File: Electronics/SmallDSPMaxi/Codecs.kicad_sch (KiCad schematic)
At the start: 56 parts, among them J13 IDC, J14 IDC, J15 IDC, J16 IDC

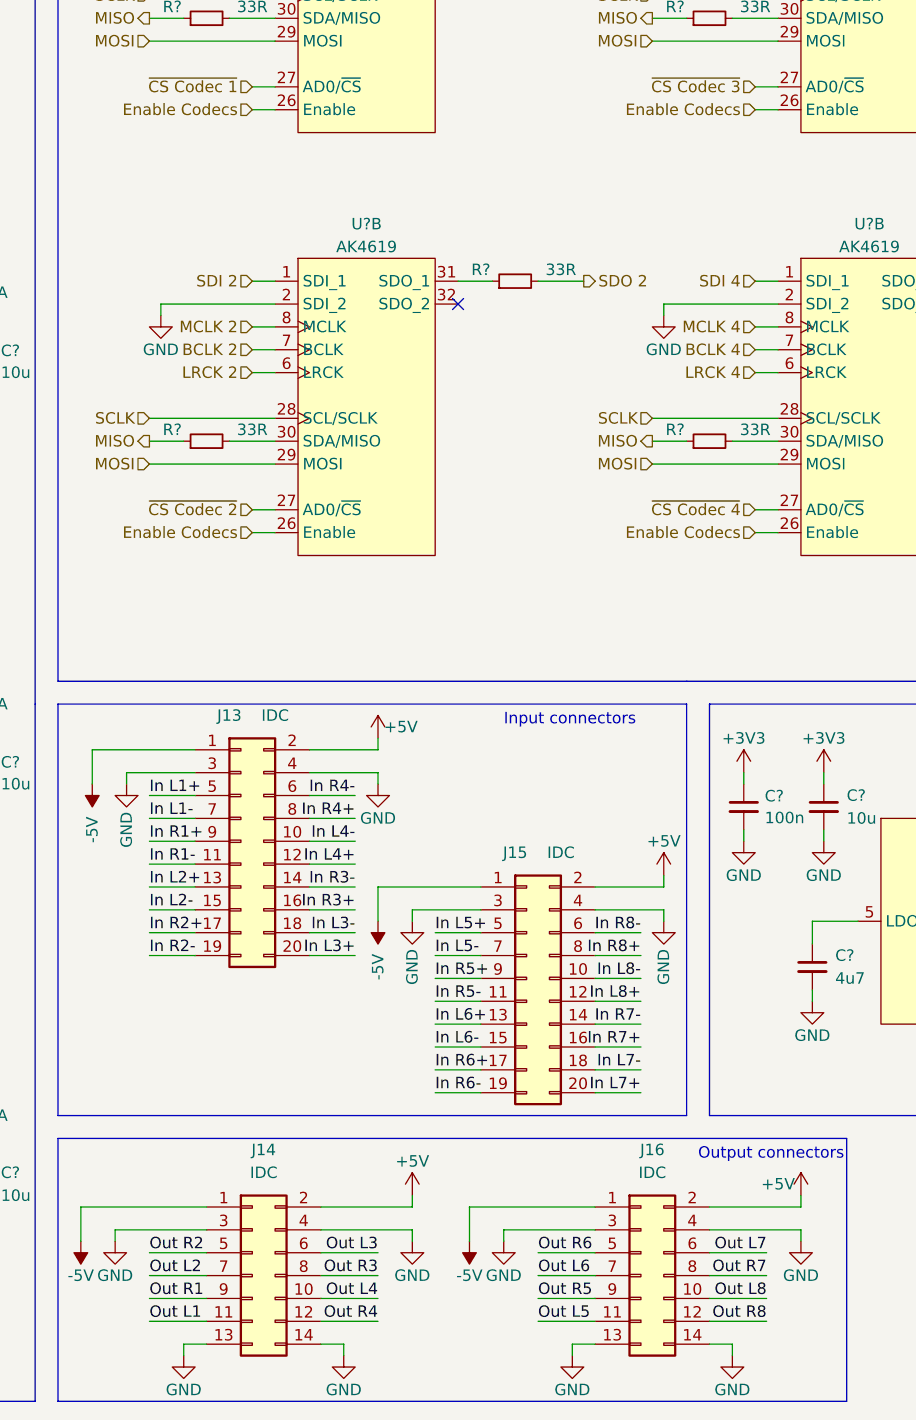
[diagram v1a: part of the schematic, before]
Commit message: Maxi: Replaces STM32 programming pin header with WE RedFit connectorand fixes minor issues. Adds driver for AKM AK4619 Codec and STM32CubeIDE workspace for Maxi firmware.
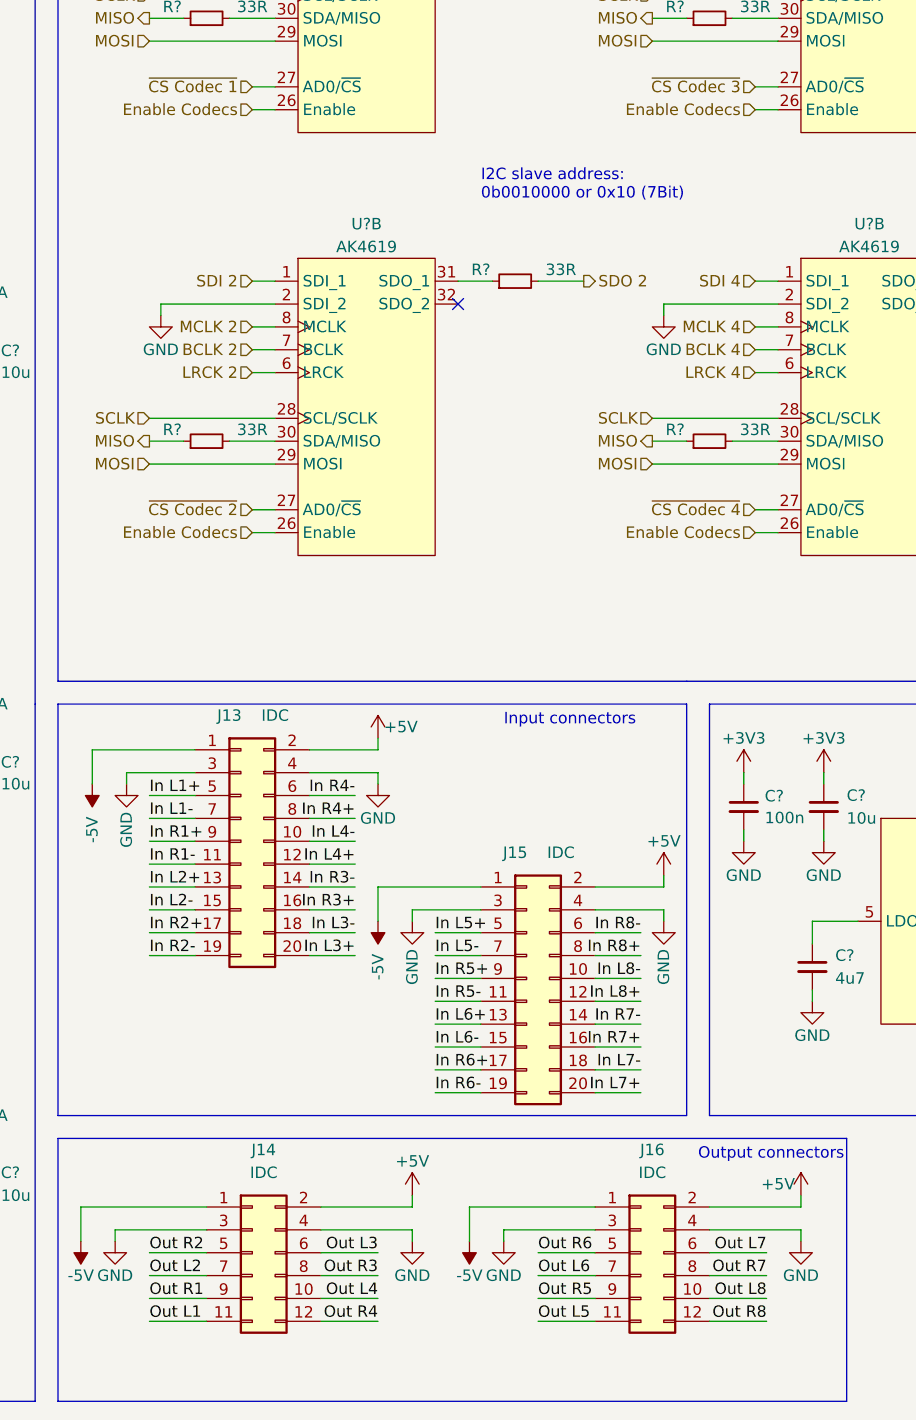
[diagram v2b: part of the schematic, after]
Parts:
- J14, J16: footprint Connector_IDC:IDC-Header_2x07_P2.54mm_Vertical -> Connector_IDC:IDC-Header_2x06_P2.54mm_Vertical; symbol Connector_Generic:Conn_02x07_Odd_Even -> Connector_Generic:Conn_02x06_Odd_Even
- U? (x12): LCSC Part # - -> C3034747; Notes (none) -> LCSC not in stock
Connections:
- net GND: no longer J14.13 (Pin_13), J14.14 (Pin_14), J16.13 (Pin_13), J16.14 (Pin_14)
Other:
- note added: "I2C slave address: 0b0010000 or 0x10 (7Bit)"

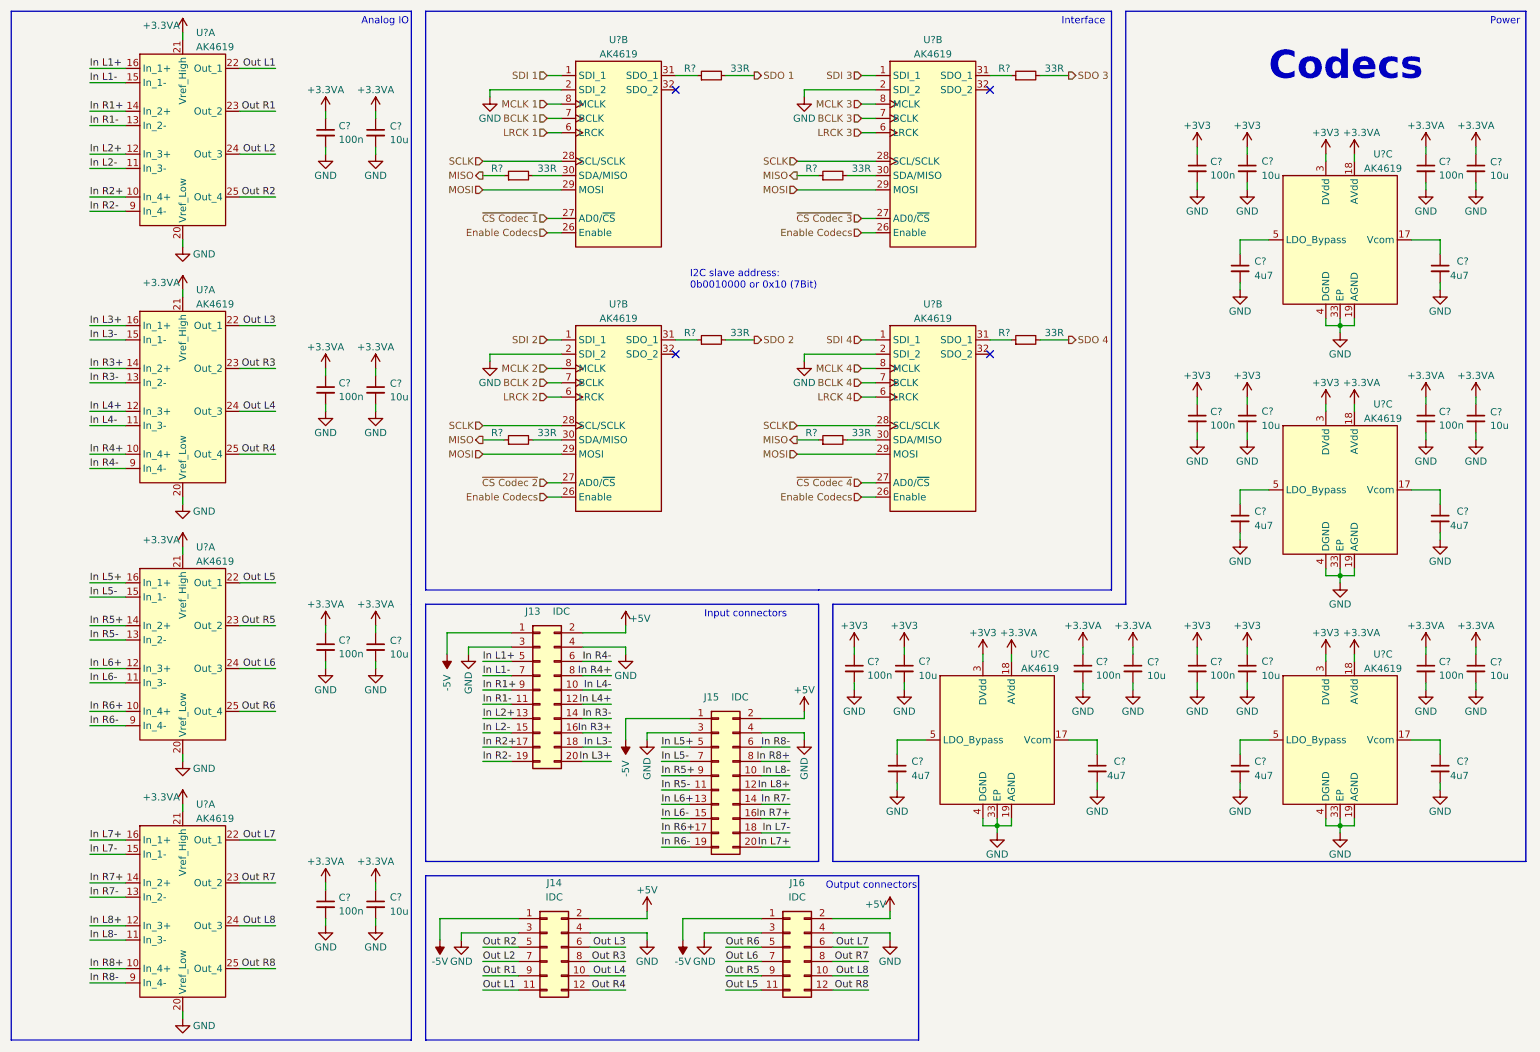
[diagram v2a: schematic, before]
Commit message: Adds AES17 measurements for rev1 of maxi. adds first iteration of maxi firmware. prototype now functional. adds mechanical information such as pcb 3d models and datasheets for psu and power switch, -connector.
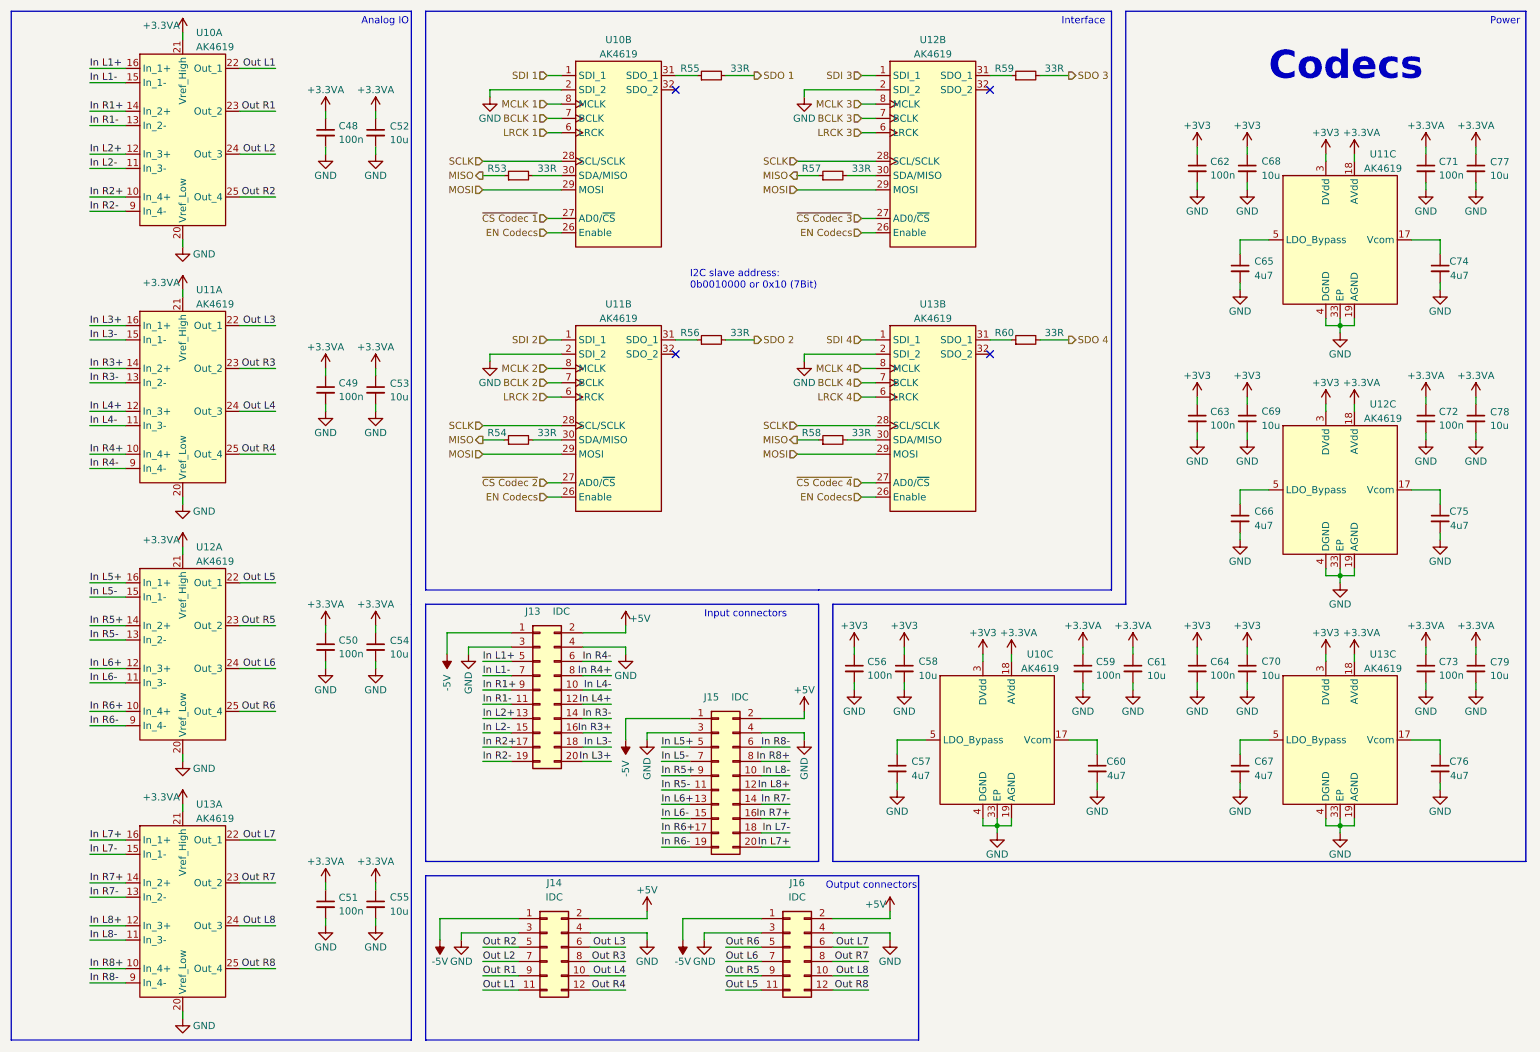
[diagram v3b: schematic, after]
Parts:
- gave numbers to parts that had none: 44
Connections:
- net Enable Codecs renamed EN Codecs
